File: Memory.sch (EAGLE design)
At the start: 13 parts, among them IC1 AT28C256ZIF, IC2 HM62256DIP, IC3 74LS139N, IC4 HM62256DIP

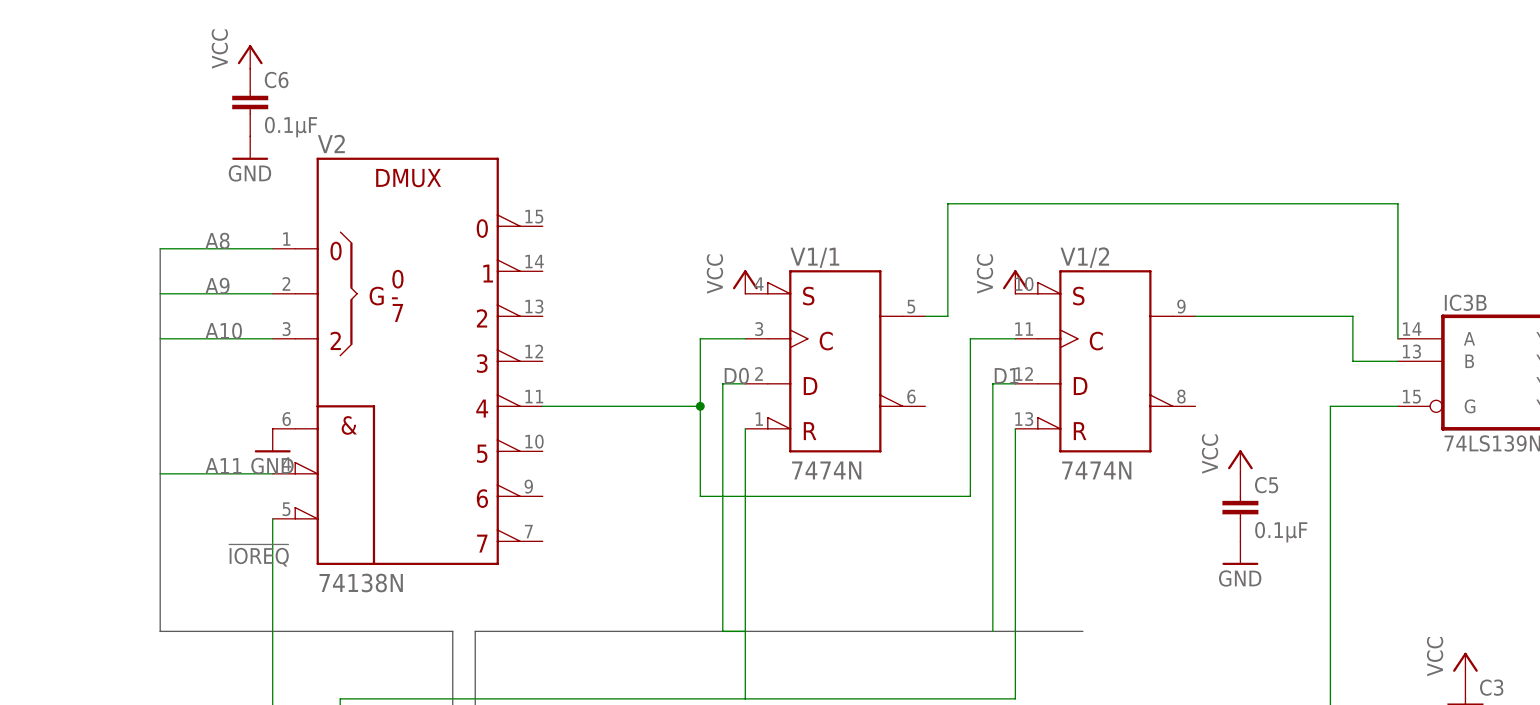
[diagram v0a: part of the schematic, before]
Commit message: Fix Missing VCC and GND Connections
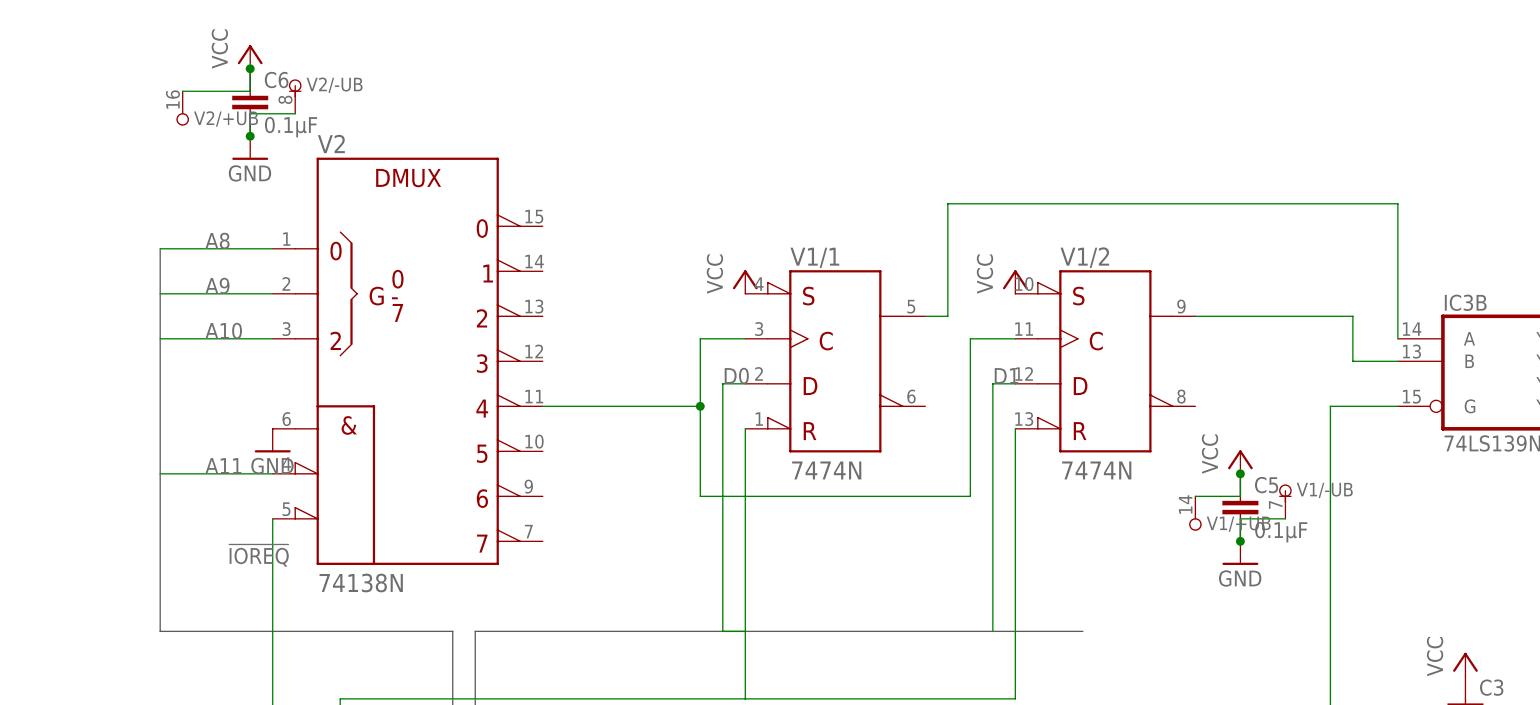
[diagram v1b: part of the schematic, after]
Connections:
- net GND: now also V1/-UB.-UB, V2/-UB.-UB
- net VCC: now also V1/+UB.+UB, V2/+UB.+UB
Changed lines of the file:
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@@
 <instance part="P+12" gate="VCC" x="-60.96" y="287.02"/>
 <instance part="GND12" gate="1" x="-60.96" y="274.32"/>
+<instance part="V2" gate="/+UB" x="-68.58" y="279.4"/>
+<instance part="V2" gate="/-UB" x="-55.88" y="281.94"/>
+<instance part="V1" gate="/+UB" x="45.72" y="233.68"/>
+<instance part="V1" gate="/-UB" x="55.88" y="236.22"/>
 </instances>
 <busses>
@@
 <pinref part="C5" gate="G$1" pin="1"/>
 <pinref part="P+11" gate="VCC" pin="VCC"/>
+<pinref part="V1" gate="/+UB" pin="+UB"/>
+<wire x1="45.72" y1="236.22" x2="50.8" y2="236.22" width="0.1524" layer="91"/>
+<wire x1="50.8" y1="236.22" x2="50.8" y2="238.76" width="0.1524" layer="91"/>
+<junction x="50.8" y="238.76"/>
 </segment>
 <segment>
 <pinref part="C6" gate="G$1" pin="1"/>
 <pinref part="P+12" gate="VCC" pin="VCC"/>
+<pinref part="V2" gate="/+UB" pin="+UB"/>
+<wire x1="-68.58" y1="281.94" x2="-60.96" y2="281.94" width="0.1524" layer="91"/>
+<wire x1="-60.96" y1="281.94" x2="-60.96" y2="284.48" width="0.1524" layer="91"/>
+<junction x="-60.96" y="284.48"/>
 </segment>
 </net>
@@
 <pinref part="C5" gate="G$1" pin="2"/>
 <pinref part="GND11" gate="1" pin="GND"/>
+<pinref part="V1" gate="/-UB" pin="-UB"/>
+<wire x1="55.88" y1="233.68" x2="50.8" y2="233.68" width="0.1524" layer="91"/>
+<wire x1="50.8" y1="233.68" x2="50.8" y2="231.14" width="0.1524" layer="91"/>
+<junction x="50.8" y="231.14"/>
 </segment>
 <segment>
 <pinref part="C6" gate="G$1" pin="2"/>
 <pinref part="GND12" gate="1" pin="GND"/>
-</segment>
-</net>
+<pinref part="V2" gate="/-UB" pin="-UB"/>
+<wire x1="-55.88" y1="279.4" x2="-60.96" y2="279.4" width="0.1524" layer="91"/>
+<wire x1="-60.96" y1="279.4" x2="-60.96" y2="276.86" width="0.1524" layer="91"/>
+<junction x="-60.96" y="276.86"/>
+</segment>
+</net>

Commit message: Add pullup
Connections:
- net GND: no longer V21.G1
- net VCC: now also V21.G1
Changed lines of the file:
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@@
 <part name="V1" library="74ttl-din" deviceset="74*74" device="N"/>
 <part name="V2" library="74ttl-din" deviceset="74*138" device="N"/>
-<part name="GND10" library="supply1" deviceset="GND" device=""/>
 <part name="P+9" library="supply1" deviceset="VCC" device=""/>
 <part name="P+10" library="supply1" deviceset="VCC" device=""/>
@@
 <part name="P+12" library="supply1" deviceset="VCC" device=""/>
 <part name="GND12" library="supply1" deviceset="GND" device=""/>
+<part name="P+13" library="supply1" deviceset="VCC" device=""/>
 </parts>
 <sheets>
@@
 <instance part="V1" gate="/2" x="35.56" y="251.46"/>
 <instance part="V2" gate="1" x="-43.18" y="251.46"/>
-<instance part="GND10" gate="1" x="-58.42" y="241.3"/>
 <instance part="IC3" gate="B" x="81.28" y="251.46"/>
 <instance part="P+9" gate="VCC" x="25.4" y="261.62"/>
@@
 <instance part="V1" gate="/+UB" x="45.72" y="233.68"/>
 <instance part="V1" gate="/-UB" x="55.88" y="236.22"/>
+<instance part="P+13" gate="VCC" x="-58.42" y="246.38"/>
 </instances>
 <busses>
@@
 <junction x="-60.96" y="284.48"/>
 </segment>
+<segment>
+<pinref part="V2" gate="1" pin="G1"/>
+<pinref part="P+13" gate="VCC" pin="VCC"/>
+</segment>
 </net>
 <net name="GND" class="0">
@@
 </segment>
 <segment>
-<pinref part="V2" gate="1" pin="G1"/>
-<pinref part="GND10" gate="1" pin="GND"/>
-</segment>
-<segment>
